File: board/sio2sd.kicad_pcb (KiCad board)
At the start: 2 copper layers, 19 parts, among them CON1 SD_Card, IC1 ATMEGA328PB-A, P1 ICSP, P2 SIO, SW1 UP, SW2 DOWN, SW3 RESET

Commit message: Single board device design
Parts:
- removed P1: ICSP, Pin_Headers:Pin_Header_Angled_1x04_Pitch2.54mm
- removed SW3: RESET, Buttons_Switches_SMD:SW_SPST_B3S-1000
- added LED1: LED2DIGIT, footprints:led2digit, F.Cu at (132.1, 99.1)
- added MISO: MISO, footprints:pad, B.Cu at (185.4, 109.2)
- added MOSI: MOSI, footprints:pad, B.Cu at (185.4, 94.0)
- added Q1: BC818-40, TO_SOT_Packages_SMD:SOT-23, B.Cu at (176.5, 113.0)
- added R10: 10k, Resistors_SMD:R_0805_HandSoldering, B.Cu at (175.3, 116.8)
- added RESET: Reset, footprints:pad, B.Cu at (185.4, 116.8)
- added SCK: SCK, footprints:pad, B.Cu at (185.4, 101.6)
- C1, C2, R1, R2, R3, R4, R5, R6, R7, R8, R9, REG1: moved to B.Cu
- CON1: footprint Connect:SD_Card_Receptacle -> footprints:sdcardsocket
- SW1, SW2: footprint Buttons_Switches_SMD:SW_SPST_B3S-1000 -> footprints:button
- moved R9 51.2 mm to (147.3, 93.3)
- moved R8 47.7 mm to (147.3, 100.3)
- moved R6 46.4 mm to (147.3, 91.4)
- moved REG1 45.7 mm to (166.4, 116.8)
- moved R4 45.5 mm to (147.3, 97.8)
- moved R5 44.6 mm to (147.3, 95.2)
- moved R3 37.6 mm to (147.3, 102.2)
- moved R1 36.1 mm to (175.3, 109.2), turned to 180 degrees
- moved R7 33.0 mm to (147.3, 104.1)
- moved P2 32.9 mm to (151.1, 109.2)
- moved R2 30.2 mm to (147.3, 106.0)
- moved C1 28.0 mm to (168.9, 111.8), turned to 180 degrees
- moved C2 25.4 mm to (168.9, 109.2), turned to 180 degrees
- moved CON1 16.6 mm to (158.8, 105.4)
- moved IC1 15.3 mm to (167.6, 100.3)
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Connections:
- CON1 pad 10: (no net) -> Net-(CON1-Pad10)
- CON1 pad 11: (no net) -> GND
- CON1 pad 12: (no net) -> GND
- CON1 pad 13: (no net) -> GND
- IC1 pad 1: (no net) -> /Digit1
- IC1 pad 27: (no net) -> /Digit0
- R1 pad 1: +3V3 -> Net-(CON1-Pad10)
- R1 pad 2: /Reset -> +3V3
- R2 pad 1: (no net) -> /Seg_A0
- R3 pad 1: (no net) -> /Seg_A2
- R4 pad 1: (no net) -> /Seg_A5
- R5 pad 1: (no net) -> /Seg_4
- R6 pad 1: (no net) -> /Seg_6
- R7 pad 1: (no net) -> /Seg_A1
- R8 pad 1: (no net) -> /Seg_A3
- R9 pad 1: (no net) -> /Seg_5
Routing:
- net Net-(IC1-Pad11): track 0.00 -> 81.3 mm, vias 0 -> 5
- net Net-(IC1-Pad12): track 0.00 -> 75.3 mm, vias 0 -> 5
- net +3V3: track 0.00 -> 56.7 mm, vias 0 -> 1
- net /Reset: track 0.00 -> 53.7 mm, vias 0 -> 4
- net /MOSI: track 0.00 -> 47.7 mm, vias 0 -> 1
- net /Digit1: track 0.00 -> 45.7 mm, vias 0 -> 3
- net /Digit0: track 0.00 -> 42.1 mm, vias 0 -> 3
- net /Seg_A2: track 0.00 -> 40.9 mm, vias 0 -> 4
- net /Seg_A3: track 0.00 -> 40.1 mm, vias 0 -> 4
- net /MISO: track 0.00 -> 39.9 mm, vias 0 -> 2
- net /SCK: track 0.00 -> 36.8 mm, vias 0 -> 1
- net /Seg_A1: track 0.00 -> 36.1 mm, vias 0 -> 4
- net /CMD: track 0.00 -> 36.0 mm, vias 0 -> 1
- net Net-(IC1-Pad10): track 0.00 -> 32.1 mm
- net /Seg_A0: track 0.00 -> 31.8 mm, vias 0 -> 3
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- added copper zone on F.Cu, net GND
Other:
- board outline added: 58.4 x 34.3 mm
- net class Default: trace_width 0.25 -> 0.3
- net class Power added: clearance 0.2, trace_width 0.5, via_dia 0.8, via_drill 0.6
- board text added: "5V"
- board text added: "CMD"
- board text added: "GND"
- board text added: "RX"
- board text added: "TX"

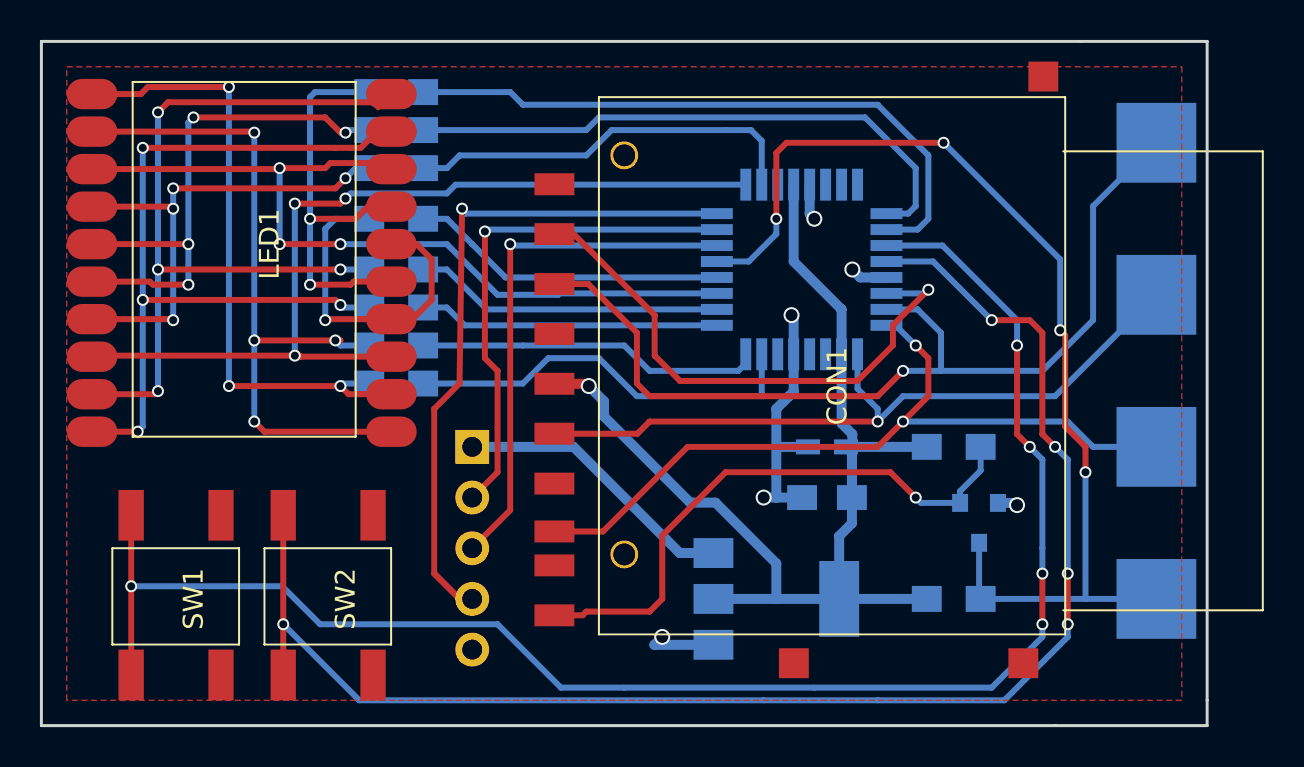
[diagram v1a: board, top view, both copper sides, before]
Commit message: Change reset circuit, layout fixes
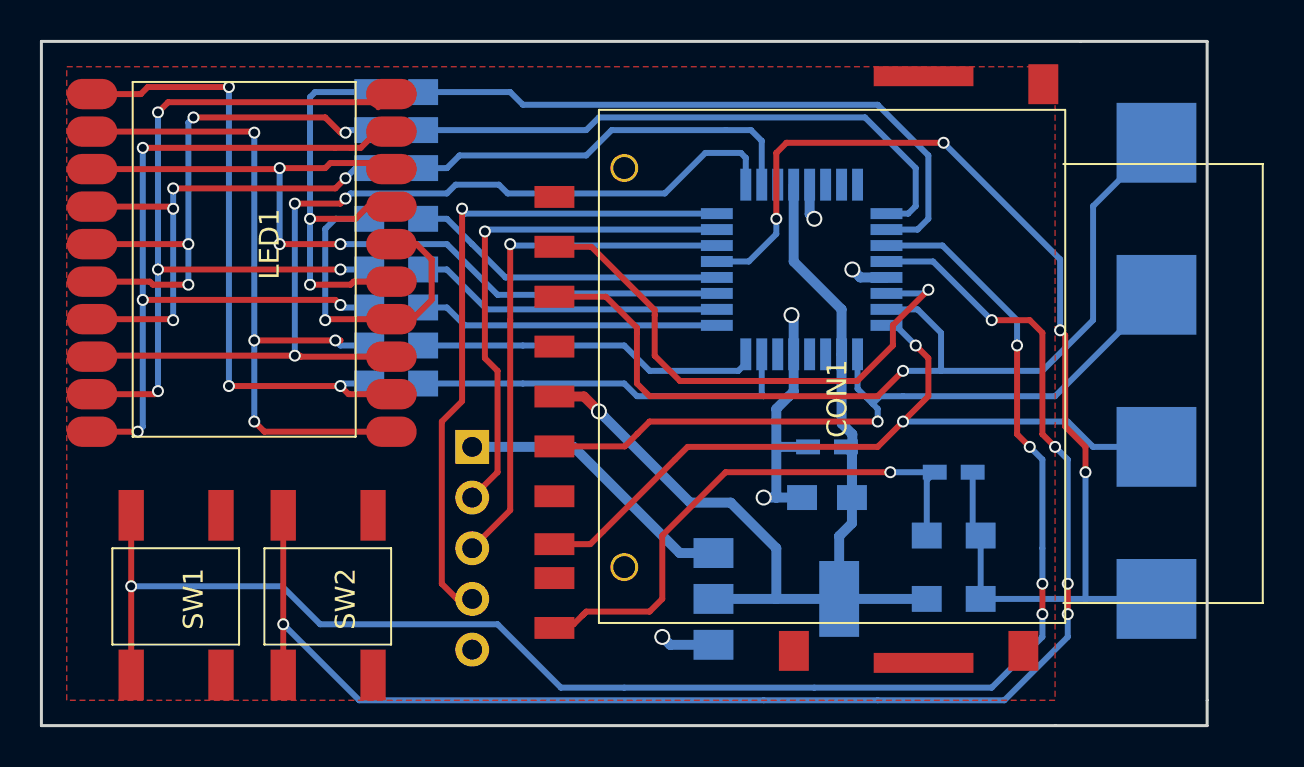
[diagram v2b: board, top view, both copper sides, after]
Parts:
- removed MISO: MISO, footprints:pad
- removed MOSI: MOSI, footprints:pad
- removed Q1: BC818-40, TO_SOT_Packages_SMD:SOT-23
- removed RESET: Reset, footprints:pad
- removed SCK: SCK, footprints:pad
- added C3: 100nF, Capacitors_SMD:C_0603_HandSoldering, B.Cu at (175.3, 110.5)
- added REF***: OSHW-Logo2_9.8x8mm_SilkScreen, Symbols:OSHW-Logo2_9.8x8mm_SilkScreen, B.Cu at (135.9, 94.6)
- added W1: MOSI, footprints:pad, B.Cu at (185.4, 94.0)
- added W2: MISO, footprints:pad, B.Cu at (185.4, 109.2)
- added W3: SCK, footprints:pad, B.Cu at (185.4, 101.6)
- added W4: Reset, footprints:pad, B.Cu at (185.4, 116.8)
- R1: value 10k -> 220k
- moved R1 4.45 mm to (175.3, 113.7), turned to 0 degrees
- moved CON1 0.64 mm to (158.8, 106.0)
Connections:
- R1 pad 2: +3V3 -> /Reset
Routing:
- net +3V3: track 56.7 -> 52.4 mm
- net /Reset: track 53.7 -> 57.5 mm
- net /Digit1: track 45.7 -> 48.1 mm
- net GND: track 21.2 -> 19.5 mm, vias 6 -> 5
- net Net-(C3-Pad2): track 29.0 -> 27.6 mm
- net /CMD: track 36.0 -> 34.6 mm
- net Net-(IC1-Pad23): track 20.5 -> 19.5 mm
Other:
- board text added: "DATA IN"
- board text added: "DATA OUT"
- board text added: "MISO"
- board text added: "MOSI"
- board text added: "RESET"
- board text added: "SCK"
- board text added: "https://github.com/ c0pperdragon/SIO2SD"
- board text removed: "RX"
- board text removed: "TX"

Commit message: Small layout fixes, Gerber files
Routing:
- net /Reset: track 57.5 -> 46.0 mm
- net Net-(IC1-Pad11): track 81.3 -> 80.3 mm, vias 5 -> 3
- net Net-(IC1-Pad12): track 75.3 -> 74.2 mm, vias 5 -> 3

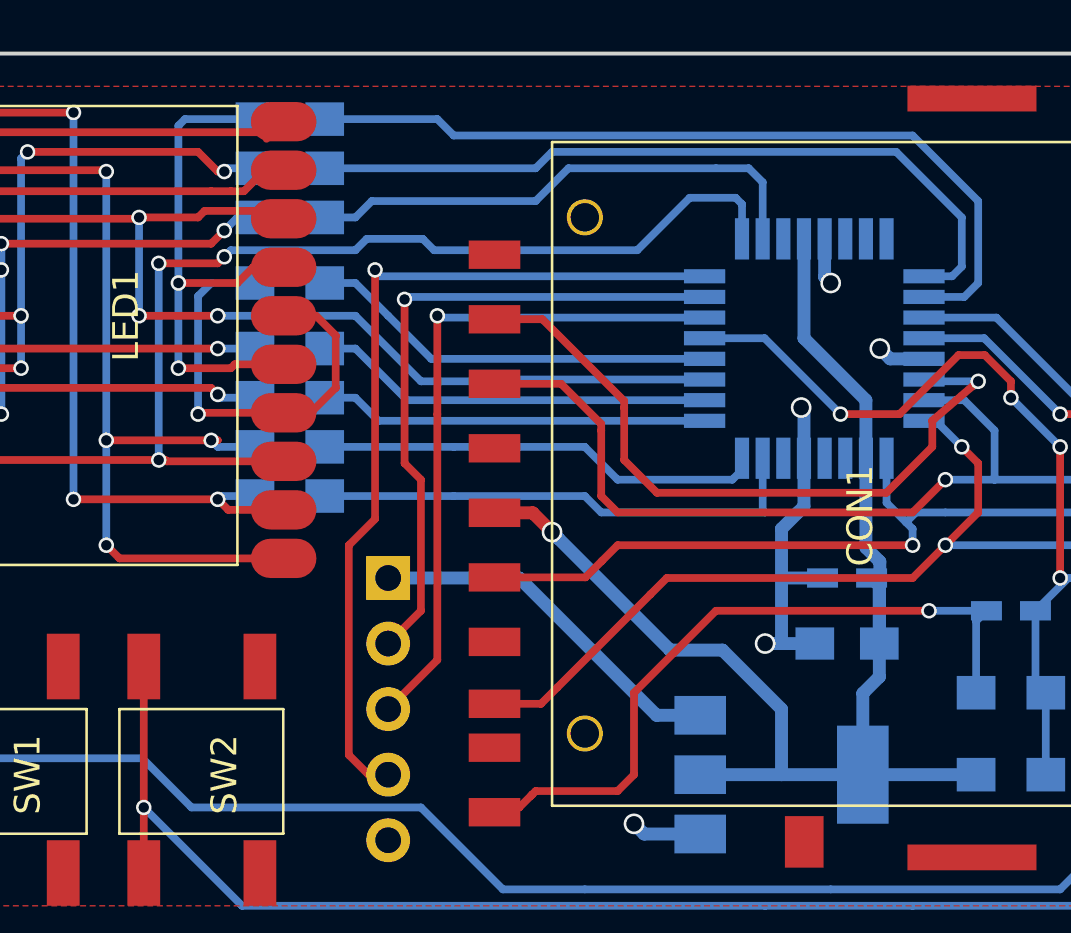
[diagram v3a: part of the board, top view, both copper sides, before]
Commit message: Allow multi-slave configuration
By inserting a diode into TX -> Data In, the device can emulate an open
collector to not interfer with other devices on the same bus.
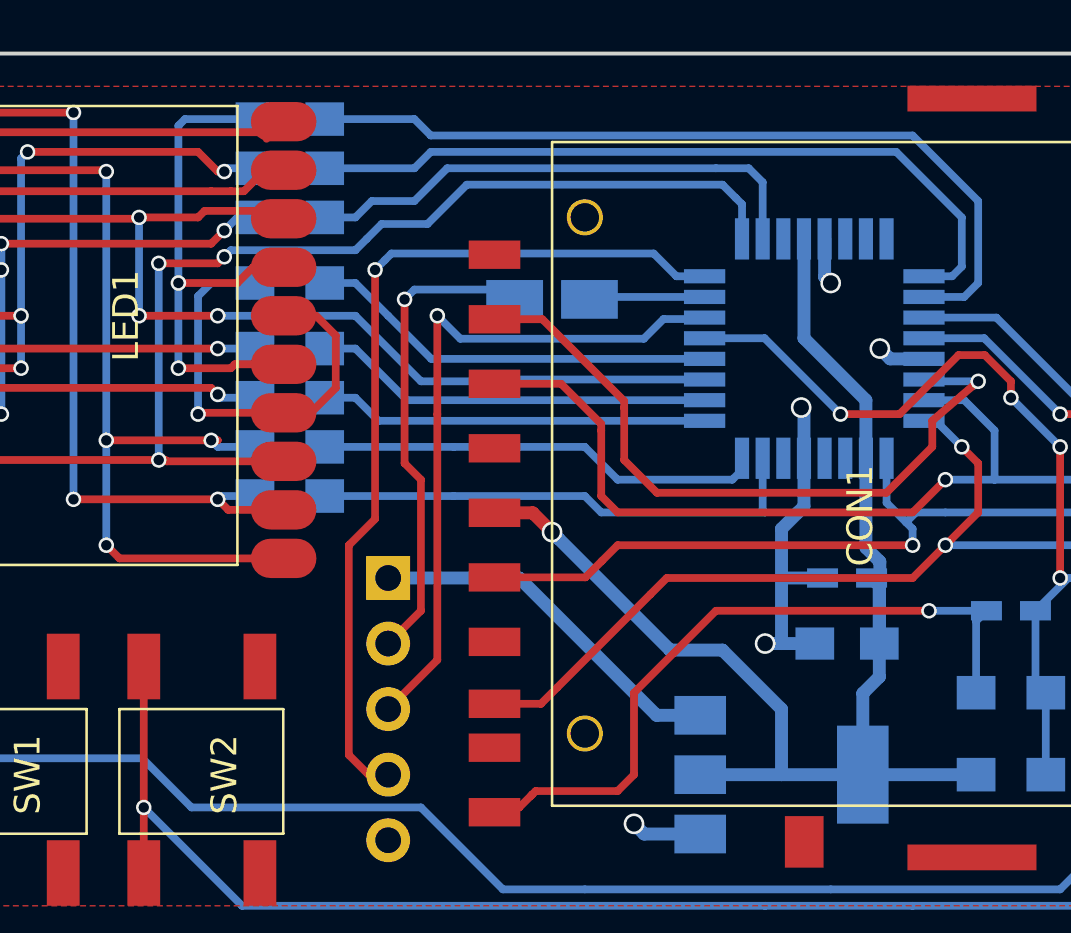
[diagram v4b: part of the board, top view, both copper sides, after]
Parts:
- added D1: 0.2V, Diodes_SMD:D_MicroMELF_Hadsoldering, B.Cu at (157.5, 98.4)
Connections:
- CON1 pad 8: (no net) -> Net-(CON1-Pad8)
- CON1 pad 9: (no net) -> Net-(CON1-Pad9)
- IC1 pad 19: (no net) -> Net-(IC1-Pad19)
- IC1 pad 20: (no net) -> Net-(IC1-Pad20)
- IC1 pad 22: (no net) -> Net-(IC1-Pad22)
- IC1 pad 3: (no net) -> Net-(IC1-Pad3)
- IC1 pad 31: /TX -> Net-(D1-Pad1)
- IC1 pad 6: (no net) -> Net-(IC1-Pad6)
- IC1 pad 7: (no net) -> Net-(IC1-Pad7)
- IC1 pad 8: (no net) -> Net-(IC1-Pad8)
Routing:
- net /TX: track 25.8 -> 18.8 mm
- net Net-(D1-Pad1): track 0.00 -> 4.50 mm
- net /RX: track 26.4 -> 27.2 mm
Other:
- board text added: "https://github.com/ c0pperdragon/SIO2SD Rev. 2"
- board text removed: "https://github.com/ c0pperdragon/SIO2SD"

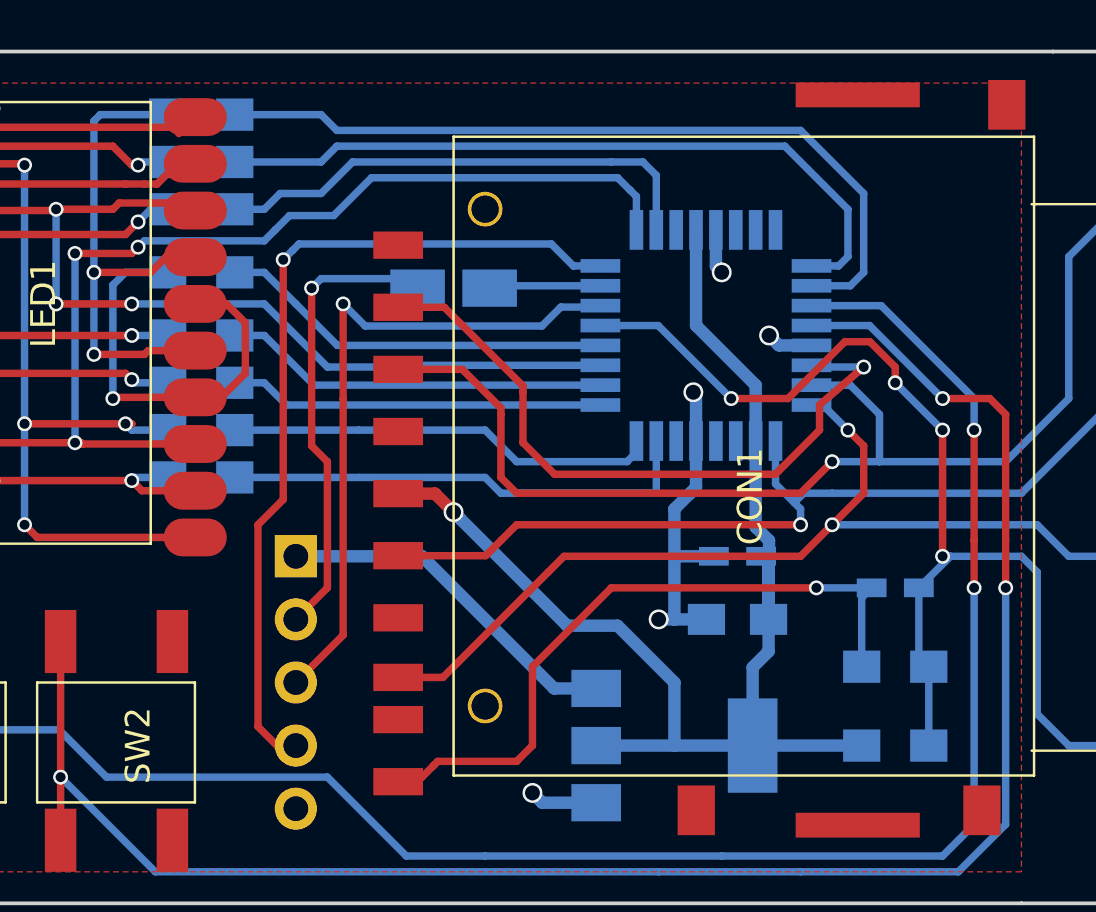
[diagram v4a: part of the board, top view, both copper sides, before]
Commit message: Bring design files to new KiCAD version. Create gerber files.
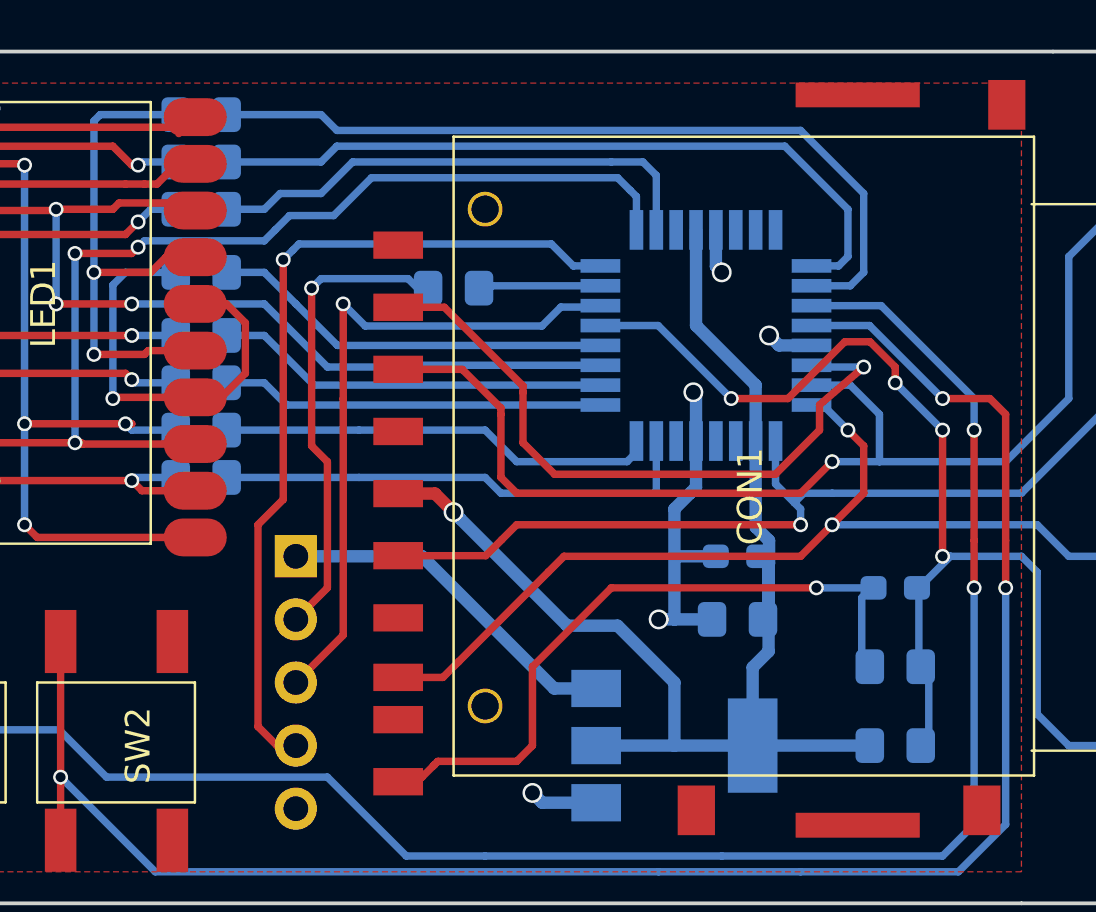
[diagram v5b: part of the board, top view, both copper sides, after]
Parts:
- C1: footprint Capacitors_SMD:C_0805_HandSoldering -> Capacitor_SMD:C_0805_2012Metric_Pad1.15x1.40mm_HandSolder
- C2, C3: footprint Capacitors_SMD:C_0603_HandSoldering -> Capacitor_SMD:C_0603_1608Metric_Pad1.05x0.95mm_HandSolder
- D1: footprint Diodes_SMD:D_MicroMELF_Hadsoldering -> Diode_SMD:D_0805_2012Metric_Pad1.15x1.40mm_HandSolder
- IC1: footprint Housings_QFP:TQFP-32_7x7mm_Pitch0.8mm -> Package_QFP:TQFP-32_7x7mm_P0.8mm
- P2: footprint Pin_Headers:Pin_Header_Angled_1x05_Pitch2.54mm -> Connector_PinHeader_2.54mm:PinHeader_1x05_P2.54mm_Horizontal
- R1, R10, R2, R3, R4, R5, R6, R7, R8, R9: footprint Resistors_SMD:R_0805_HandSoldering -> Resistor_SMD:R_0805_2012Metric_Pad1.15x1.40mm_HandSolder
- REG1: footprint TO_SOT_Packages_SMD:SOT-223 -> Package_TO_SOT_SMD:SOT-223
